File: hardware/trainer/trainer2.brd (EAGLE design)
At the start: 86 x 56 mm, 53 parts, among them Q1 2N3906, Q2 2N3906, Q3 2N3906, Q4 2N3906

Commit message: Añado trainer2
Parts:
- removed D5: 1N4148DO35-7, diode:DO35-7
- added 10, 5, 6, B, G, H, T, V, Y: (no value), switch-tact:DTS-6
- added D0: (no value), diode:DO35-7
- added JP1: (no value), pinhead:1X01
- D1, D2, D3, D4: value 1N4148DO35-7 -> (none)
- RN1, RN2: value 2K2 -> 100
- RN4: value (none) -> 2K2
- moved LED1 78.1 mm to (79.6, 27.7), turned to 0 degrees
- moved LED2 73.8 mm to (76.9, 24.1), turned to 0 degrees
- moved LED3 73.6 mm to (79.7, 20.7), turned to 0 degrees
- moved LED4 70.2 mm to (77.0, 17.1), turned to 0 degrees
- moved LED5 69.9 mm to (79.5, 13.4), turned to 0 degrees
- moved Q3 69.3 mm to (99.3, 27.0), turned to 180 degrees
- moved RN3 69.3 mm to (73.4, 20.8), turned to 90 degrees
- moved RN4 67.8 mm to (98.0, 21.9), turned to 180 degrees
- moved Q4 58.2 mm to (86.6, 27.0), turned to 180 degrees
- moved Q2 56.4 mm to (105.6, 27.0), turned to 180 degrees
- moved SW1 39.7 mm to (11.4, 34.4), turned to 0 degrees
- moved Q1 39.3 mm to (92.9, 27.0), turned to 180 degrees
- moved RN2 21.4 mm to (65.5, 36.2)
- moved RN1 20.7 mm to (65.3, 41.6)
- moved 0 14.7 mm to (68.4, 25.2)
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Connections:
- removed net N$33 (its old number): RN2.7, U$2.4
- removed net N$34 (its old number): RN2.5, U$2.2
- removed net N$35 (its old number): RN2.1, U$2.1
- removed net N$36 (its old number): RN1.3, U$2.10
- new net N$11: RN1.5, U$2.4
- new net N$12: RN2.7, U$2.2
- new net N$13: RN2.5, U$2.1
- new net N$14: RN2.1, U$2.10
- new net N$15: 10.3, JP1.1
- new net N$28: B.2, V.1
- new net N$29: 5.1, T.2
- new net N$40: 7.1, U.2
- new net N$42: G.1, V.2
- new net N$45: SW1.1, SW1.2, SW1.3, SW1.4, SW1.5, SW1.6, SW1.7, SW1.8
- new net N$50: B.1, H.2
- new net N$51: H.1, Y.2
- new net N$55: 6.2, Y.1
- new net N$56: 9.1, O.2
- net A10: now also SW1.14, T.4; no longer SW1.10
- net A11: now also 5.4, SW1.13; no longer SW1.9
- net A12: now also 6.3, SW1.12; no longer SW1.4
- net A13: now also SW1.11, Y.3; no longer SW1.3
- net A14: now also H.3, SW1.10; no longer SW1.2
- net A15: now also B.3, SW1.9; no longer SW1.1
- net A8: now also SW1.16, V.4; no longer SW1.12
- net A9: now also G.4, SW1.15; no longer SW1.11
- net D0: now also D0.A; no longer D5.A
- net D1: now also D1.A; no longer 9.1, D4.A, O.2
- net D2: now also D2.A; no longer D3.A
- net D3: now also D3.A; no longer D2.A
- net D4: now also 5.2, D4.A; no longer D1.A, SW1.13, SW1.14, SW1.15, SW1.16, SW1.5, SW1.6, SW1.7, SW1.8
- net DIG1: now also U$1.P19; no longer U$1.P18
- net DIG3: now also U$1.P18; no longer U$1.P17
- net DIG4: now also U$1.P23; no longer U$1.P26
- net DISB: now also RN1.4; no longer RN1.6
- net DISC: now also RN1.6; no longer RN2.8
- net DISD: now also U$1.P33; no longer U$1.P34
- net DISDP: now also RN2.8, U$1.P6; no longer RN2.2, U$1.P10
- net DISE: now also RN2.2; no longer RN1.4
- net DISF: now also U$1.P17; no longer U$1.P19
- net DISG: now also U$1.P12; no longer U$1.P15
- net GND: now also 10.1
- net LED1: no longer U$1.P35
- net LED2: no longer U$1.P32
- net LED3: now also U$1.P32; no longer U$1.P33
- net LED4: now also U$1.P26; no longer U$1.P23
- net LED6: now also U$1.P24; no longer U$1.P20
- net N$10: now also RN1.3, U$2.7; no longer 7.2, U.2
- net N$30: now also G.2, T.1; no longer RN1.5, U$2.7
- net PUSH2: now also U$1.P20; no longer U$1.P24
- net SW1: now also U$1.P9; no longer U$1.P6
- net SW4: now also U$1.P11; no longer U$1.P9
- net SW5: now also U$1.P10; no longer U$1.P11
- net SW6: now also U$1.P14; no longer U$1.P12
- net SW7: now also U$1.P15; no longer U$1.P14
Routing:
- net N$22: track 86.8 -> 0.00 mm
- net N$19: track 61.5 -> 0.00 mm
- net ELETE: track 58.4 -> 0.00 mm
- net A13: track 44.1 -> 0.00 mm
- net N$43: track 33.4 -> 0.00 mm
- net A11: track 31.1 -> 0.00 mm
- net A8: track 31.1 -> 0.00 mm
- net A10: track 31.1 -> 0.00 mm
- net A9: track 31.1 -> 0.00 mm
- net N$30: track 29.0 -> 0.00 mm
- net N$9: track 28.6 -> 0.00 mm
- net N$36 (its old number): track 26.4 -> 0.00 mm
- net A12: track 20.3 -> 0.00 mm
- net N$54: track 2.07 -> 0.00 mm
- net N$53: track 2.07 -> 0.00 mm
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- added copper zone on layer 1, net GND
- added copper zone on layer 16, net GND
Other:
- board size 86 x 56 mm -> 82.1 x 54.3 mm
- board text removed: "AntonioVillena 04/2015"
- board text removed: "Tecleator v1.1"

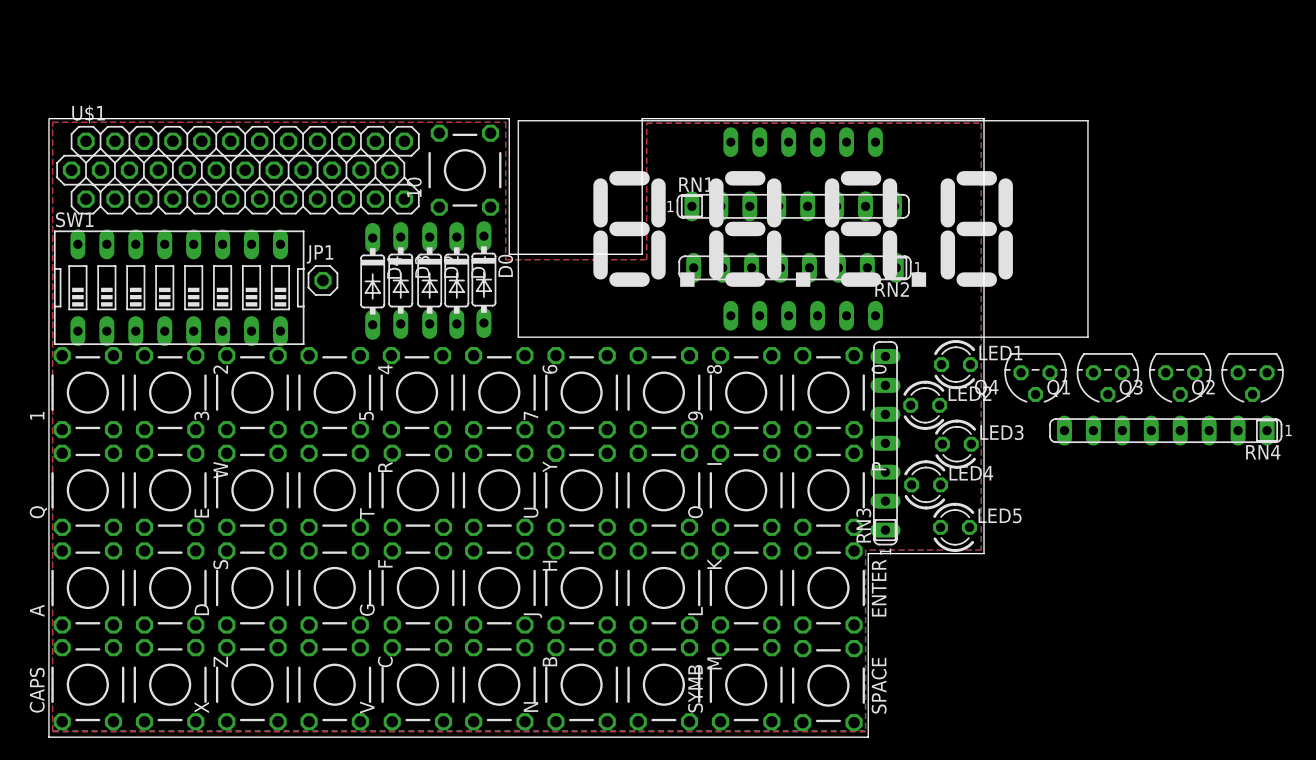
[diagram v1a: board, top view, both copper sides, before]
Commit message: Actualizo ruteado de trainer2
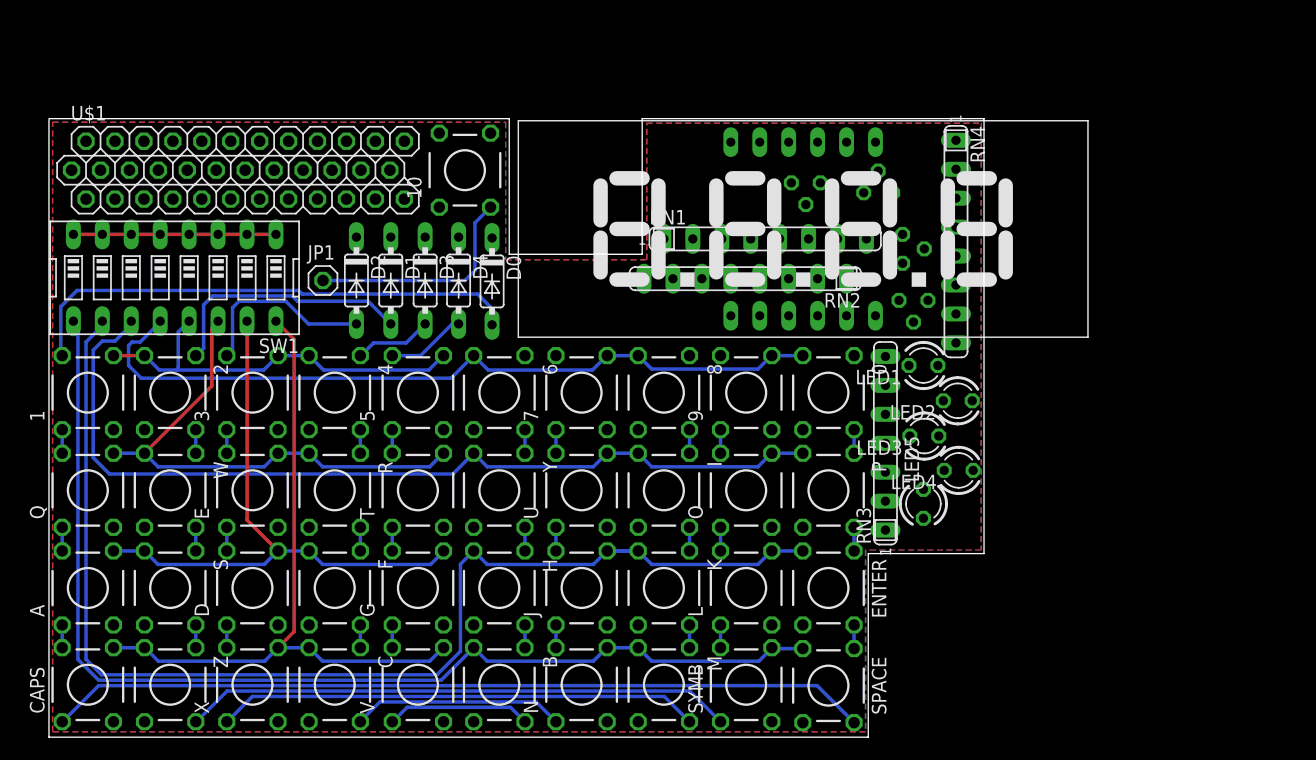
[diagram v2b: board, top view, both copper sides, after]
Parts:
- moved Q3 36.8 mm to (66.4, 43.7), flipped to the bottom
- moved Q2 36.5 mm to (72.8, 42.8), flipped to the bottom, turned to 0 degrees
- moved RN4 24.8 mm to (79.6, 38.5), turned to 270 degrees
- moved Q1 21.0 mm to (74.9, 37.9), flipped to the bottom, turned to 90 degrees
- moved Q4 12.5 mm to (75.9, 33.3), flipped to the bottom
- moved D4 7.54 mm to (36.0, 35.1)
- moved D2 6.43 mm to (27.0, 35.1)
- moved D1 5.79 mm to (30.0, 35.1)
- moved RN2 4.47 mm to (61.1, 35.2)
- moved RN1 3.77 mm to (62.9, 38.7)
- moved LED5 3.46 mm to (76.8, 15.5), turned to 90 degrees
- moved LED4 3.13 mm to (79.9, 18.4), turned to 180 degrees
- moved LED3 2.95 mm to (76.8, 21.4), turned to 180 degrees
- moved LED2 2.88 mm to (79.8, 24.5), turned to 180 degrees
- moved LED1 2.86 mm to (76.8, 27.6), turned to 180 degrees
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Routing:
- net A14: track 0.00 -> 107.4 mm
- net A15: track 0.00 -> 97.4 mm
- net A13: track 0.00 -> 79.6 mm
- net N$22: track 0.00 -> 72.2 mm
- net A12: track 0.00 -> 68.0 mm
- net A8: track 0.00 -> 60.8 mm
- net A9: track 0.00 -> 52.3 mm
- net N$19: track 0.00 -> 48.3 mm
- net A10: track 0.00 -> 45.2 mm
- net D0: track 0.00 -> 44.9 mm
- net ELETE: track 0.00 -> 42.5 mm
- net A11: track 0.00 -> 35.8 mm
- net D1: track 0.00 -> 22.5 mm
- net N$15: track 0.00 -> 19.8 mm
- net N$43: track 0.00 -> 18.6 mm
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
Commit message: Actualizo trainer2
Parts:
- turned 10 to 270 degrees
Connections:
- removed net LED6: U$1.P24
- removed net N$45: SW1.1, SW1.2, SW1.3, SW1.4, SW1.5, SW1.6, SW1.7, SW1.8
- removed net PUSH1: U$1.P29
- removed net PUSH2: U$1.P20
- removed net PUSH3: U$1.P27
- removed net PUSH4: U$1.P30
- removed net SW1: U$1.P9
- removed net SW2: U$1.P8
- removed net SW3: U$1.P7
- removed net SW4: U$1.P11
- removed net SW5: U$1.P10
- removed net SW6: U$1.P14
- removed net SW7: U$1.P15
- removed net SW8: U$1.P13
- new net COL0: D0.C, U$1.P35
- new net COL1: D1.C, U$1.P32
- new net COL2: D2.C, U$1.P31
- new net COL3: D3.C, U$1.P33
- new net COL4: D4.C, U$1.P34
- net A10: now also U$1.P14
- net A11: now also U$1.P10
- net A12: now also U$1.P11
- net A13: now also U$1.P7
- net A14: now also U$1.P8
- net A15: now also U$1.P6
- net A8: now also U$1.P9
- net A9: now also U$1.P13
- net DIG1: now also U$1.P22; no longer U$1.P19
- net DIG2: now also U$1.P15; no longer U$1.P16
- net DISA: now also U$1.P27; no longer U$1.P25
- net DISC: now also U$1.P25; no longer U$1.P31
- net DISD: now also U$1.P30; no longer U$1.P33
- net DISDP: now also U$1.P26; no longer U$1.P6
- net DISE: now also U$1.P24; no longer U$1.P22
- net DISF: now also U$1.P29; no longer U$1.P17
- net DISG: now also U$1.P21; no longer U$1.P12
- net GND: now also 10.2, SW1.1, SW1.2, SW1.3, SW1.4, SW1.5, SW1.6, SW1.7, SW1.8; no longer 10.1
- net LED1: now also U$1.P20
- net LED2: now also U$1.P19
- net LED3: now also U$1.P17; no longer U$1.P32
- net LED4: now also U$1.P16; no longer U$1.P26
- net LED5: now also U$1.P12; no longer U$1.P21
- net N$15: now also 10.4; no longer 10.3
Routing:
- net GND: track 0.00 -> 110.3 mm
- net LED5: track 0.00 -> 90.3 mm
- net LED4: track 0.00 -> 88.7 mm
- net LED3: track 0.00 -> 80.1 mm
- net LED2: track 0.00 -> 75.0 mm
- net LED1: track 0.00 -> 72.7 mm
- net A8: track 60.8 -> 84.4 mm
- net N$45: track 17.8 -> 0.00 mm
- net A15: track 97.4 -> 114.6 mm
- net A10: track 45.2 -> 60.6 mm
- net COL0: track 0.00 -> 14.6 mm
- net A12: track 68.0 -> 82.3 mm
- net A14: track 107.4 -> 121.5 mm
- net A9: track 52.3 -> 65.7 mm
- net A11: track 35.8 -> 48.2 mm
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
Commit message: Penúltimo avance trainer
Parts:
- moved Q2 0.32 mm to (72.8, 42.5)
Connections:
- net COL0: now also U$1.P21; no longer U$1.P35
- net COL1: now also U$1.P18; no longer U$1.P32
- net COL3: now also U$1.P15; no longer U$1.P33
- net DIG2: now also U$1.P33; no longer U$1.P15
- net DIG3: now also U$1.P24; no longer U$1.P18
- net DISA: now also U$1.P32; no longer U$1.P27
- net DISB: now also U$1.P29; no longer U$1.P28
- net DISC: now also U$1.P27; no longer U$1.P25
- net DISD: now also U$1.P25; no longer U$1.P30
- net DISDP: now also U$1.P35; no longer U$1.P26
- net DISE: now also U$1.P26; no longer U$1.P24
- net DISF: now also U$1.P28; no longer U$1.P29
- net DISG: now also U$1.P30; no longer U$1.P21
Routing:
- net DIG4: track 0.00 -> 79.7 mm
- net DIG1: track 0.00 -> 76.7 mm
- net DIG3: track 0.00 -> 76.7 mm
- net DIG2: track 0.00 -> 71.0 mm
- net VCC: track 0.00 -> 70.1 mm
- net DISD: track 0.00 -> 67.4 mm
- net DISC: track 0.00 -> 64.1 mm
- net DISE: track 0.00 -> 60.3 mm
- net DISB: track 0.00 -> 50.9 mm
- net DISF: track 0.00 -> 46.5 mm
- net DISG: track 0.00 -> 45.0 mm
- net DISA: track 0.00 -> 43.9 mm
- net DISDP: track 0.00 -> 31.2 mm
- net COL3: track 11.8 -> 28.8 mm
- net N$7: track 0.00 -> 16.4 mm
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
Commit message: Acabo trainer2
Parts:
- removed U$1: ZXUNO_CONNECTOR, zxuno:ZXUNO_CONNECTOR
- added EDGE: ZXUNO_CONNECTOR, zxuno:ZXUNO_CONNECTOR
- moved LED1 5.00 mm to (76.8, 32.6)
- moved LED3 5.00 mm to (76.8, 26.4)
- moved A 5.00 mm to (3.41, 13.1)
- moved D 5.00 mm to (17.9, 13.1)
- moved ENTER 5.00 mm to (68.4, 13.1)
- moved F 5.00 mm to (25.1, 13.1)
- moved G 5.00 mm to (32.4, 13.1)
- moved H 5.00 mm to (39.5, 13.1)
- moved J 5.00 mm to (46.8, 13.1)
- moved K 5.00 mm to (54.0, 13.1)
- moved L 5.00 mm to (61.2, 13.1)
- moved LED5 5.00 mm to (76.8, 20.5)
- moved S 5.00 mm to (10.6, 13.1)
- moved SPACE 5.00 mm to (68.4, 4.52)
- moved 0 5.00 mm to (68.4, 30.2)
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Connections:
- net 3.3V: now also EDGE.3.3V@1; no longer U$1.3.3V@1
- net 5V: now also EDGE.5V; no longer U$1.5V
- net A10: now also EDGE.P14; no longer U$1.P14
- net A11: now also EDGE.P10; no longer U$1.P10
- net A12: now also EDGE.P11; no longer U$1.P11
- net A13: now also EDGE.P7; no longer U$1.P7
- net A14: now also EDGE.P8; no longer U$1.P8
- net A15: now also EDGE.P6; no longer U$1.P6
- net A8: now also EDGE.P9; no longer U$1.P9
- net A9: now also EDGE.P13; no longer U$1.P13
- net COL0: now also EDGE.P21; no longer U$1.P21
- net COL1: now also EDGE.P18; no longer U$1.P18
- net COL2: now also EDGE.P31; no longer U$1.P31
- net COL3: now also EDGE.P15; no longer U$1.P15
- net COL4: now also EDGE.P34; no longer U$1.P34
- net DIG1: now also EDGE.P22; no longer U$1.P22
- net DIG2: now also EDGE.P33; no longer U$1.P33
- net DIG3: now also EDGE.P24; no longer U$1.P24
- net DIG4: now also EDGE.P23; no longer U$1.P23
- net DISA: now also EDGE.P32; no longer U$1.P32
- net DISB: now also EDGE.P29; no longer U$1.P29
- net DISC: now also EDGE.P27; no longer U$1.P27
- net DISD: now also EDGE.P25; no longer U$1.P25
- net DISDP: now also EDGE.P35; no longer U$1.P35
- net DISE: now also EDGE.P26; no longer U$1.P26
- net DISF: now also EDGE.P28; no longer U$1.P28
- net DISG: now also EDGE.P30; no longer U$1.P30
- net GND: now also EDGE.GND@1, EDGE.GND@2; no longer U$1.GND@1, U$1.GND@2
- net LED1: now also EDGE.P20; no longer U$1.P20
- net LED2: now also EDGE.P19; no longer U$1.P19
- net LED3: now also EDGE.P17; no longer U$1.P17
- net LED4: now also EDGE.P16; no longer U$1.P16
- net LED5: now also EDGE.P12; no longer U$1.P12
- net VCC: now also EDGE.3.3V@2; no longer U$1.3.3V@2
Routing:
- net N$4: track 0.00 -> 30.6 mm
- net N$10: track 0.00 -> 24.5 mm
- net N$14: track 0.00 -> 17.6 mm
- net N$9: track 0.00 -> 13.6 mm
- net DIG4: track 79.7 -> 84.0 mm
- net N$1: track 10.4 -> 8.13 mm
- net DIG3: track 76.7 -> 77.9 mm
